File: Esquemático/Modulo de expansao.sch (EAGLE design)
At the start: 77 parts, among them K1 AQYAQY27, K2 AQYAQY27, K3 AQYAQY27, K4 AQYAQY27, K5 AQYAQY27, K6 AQYAQY27, U3 LM1117-3.3V

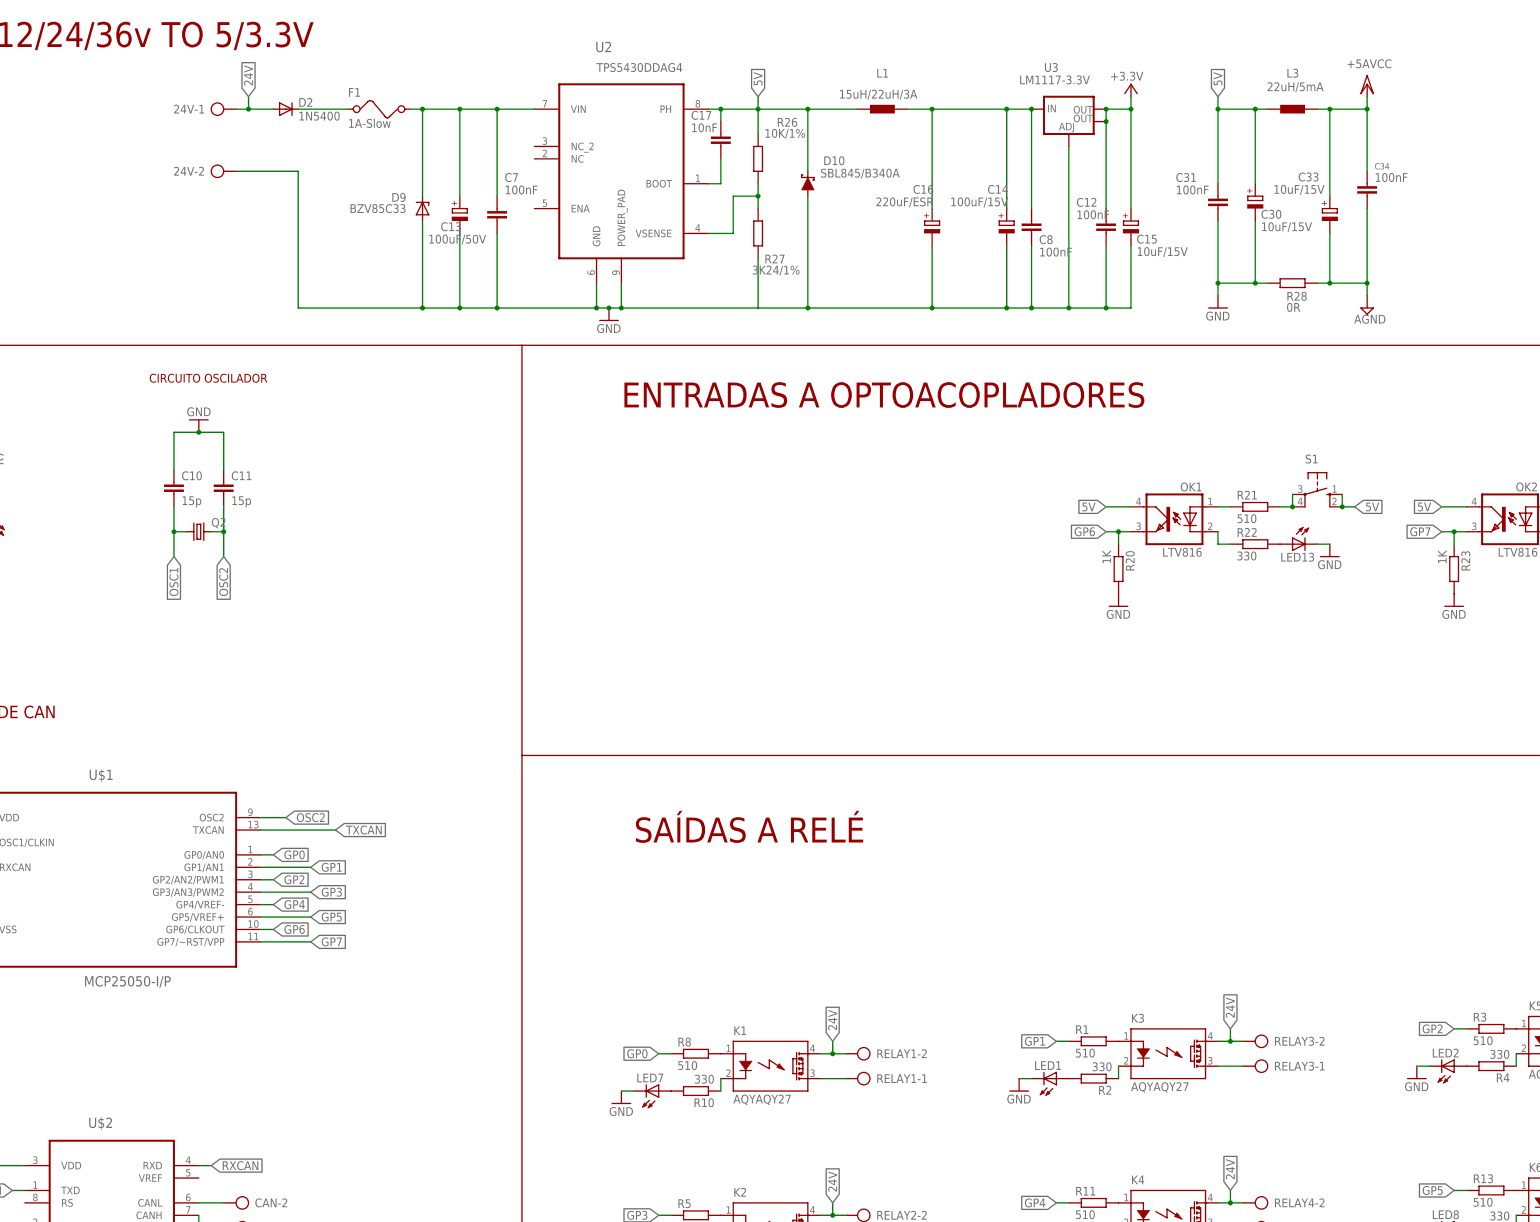
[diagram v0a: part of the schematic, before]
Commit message: Correçao no modulo de expansao e alteraçao de nomes dos ficheiros
No modulo de expansao, passei tudo para thro hole e comecei já a fazer
pcb. enviei para o isaias por email para ver se quer alterar alguma
coisa
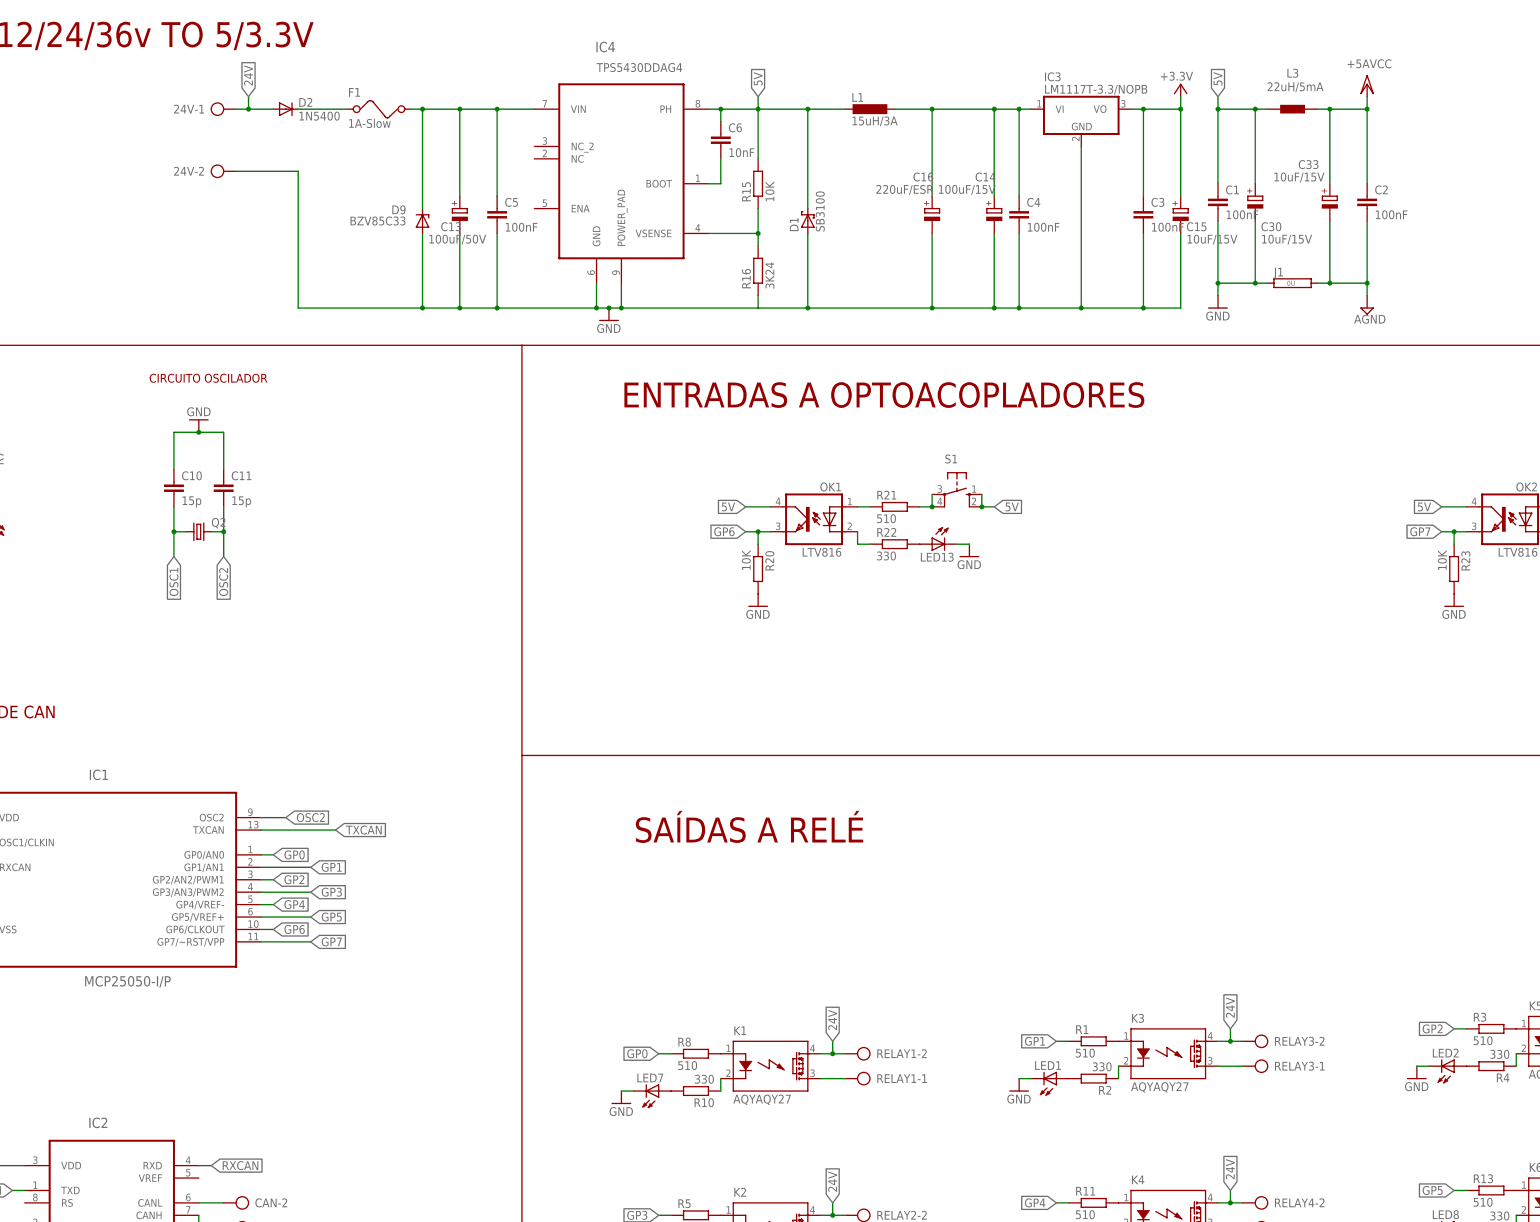
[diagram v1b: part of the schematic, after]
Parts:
- removed C12, C31, C34, C7, C8: 100nF, rcl:C-EUC0805
- removed C17: 10nF, rcl:C-EUC0805
- removed D10: SBL845/B340A, SparkFun-DiscreteSemi:DIODE-SCHOTTKY-B340A
- removed R26: 10K/1%, rcl:R-EU_R0603
- removed R27: 3K24/1%, rcl:R-EU_R0603
- removed R28: 0R, rcl:R-EU_R0603
- removed U3: LM1117-3.3V, SparkFun-IC-Power:V_REG_LM1117SOT223
- added C1, C2, C3, C4, C5: 100nF, rcl:C-EU050-024X044
- added C6: 10nF, rcl:C-EU075-032X103
- added D1: SB3100, diode:1N5908
- added IC3: LM1117T-3.3/NOPB, linear:LM340H-12
- added J1: (no value), jumper:0R
- added R15: 10K, rcl:R-EU_0204/7
- added R16: 3K24, rcl:R-EU_0204/7
- L1: value 15uH/22uH/3A -> 15uH/3A; device inductors:DR1030 -> rcl:L-EUTJ3-U1
- R20, R23: value 1K -> 10K
- renumbered U$1 to IC1, U$2 to IC2, U2 to IC4
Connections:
- net +3.3V: now also C3.1, IC3.VO; no longer C12.1, U3.OUT, U3.OUT@1
- net 5V: now also C1.1, C6.1, D1.C, L1.2, R15.2; no longer C17.1, C31.1, D10.C, L1.1, R26.1
- net AGND: now also C2.2, J1.2; no longer C34.2, R28.2
- net GND: now also C1.2, C3.2, C4.2, C5.2, D1.A, IC3.GND, J1.1, R16.1; no longer C12.2, C31.2, C7.2, C8.2, D10.A, R27.2, R28.1, U3.ADJ
- net N$21: now also C5.1; no longer C7.1
- net N$65: now also C4.1, IC3.VI, L1.1; no longer C8.1, L1.2, U3.IN
- net N$66: now also C6.2; no longer C17.2
- net N$67: now also R15.1, R16.2; no longer R26.2, R27.1
- net VCC/2: now also C2.1; no longer C34.1
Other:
- moved on the sheet: C14, C15, C16, C33, D9, L1, LED13, OK1, R20, R21, R22, S1

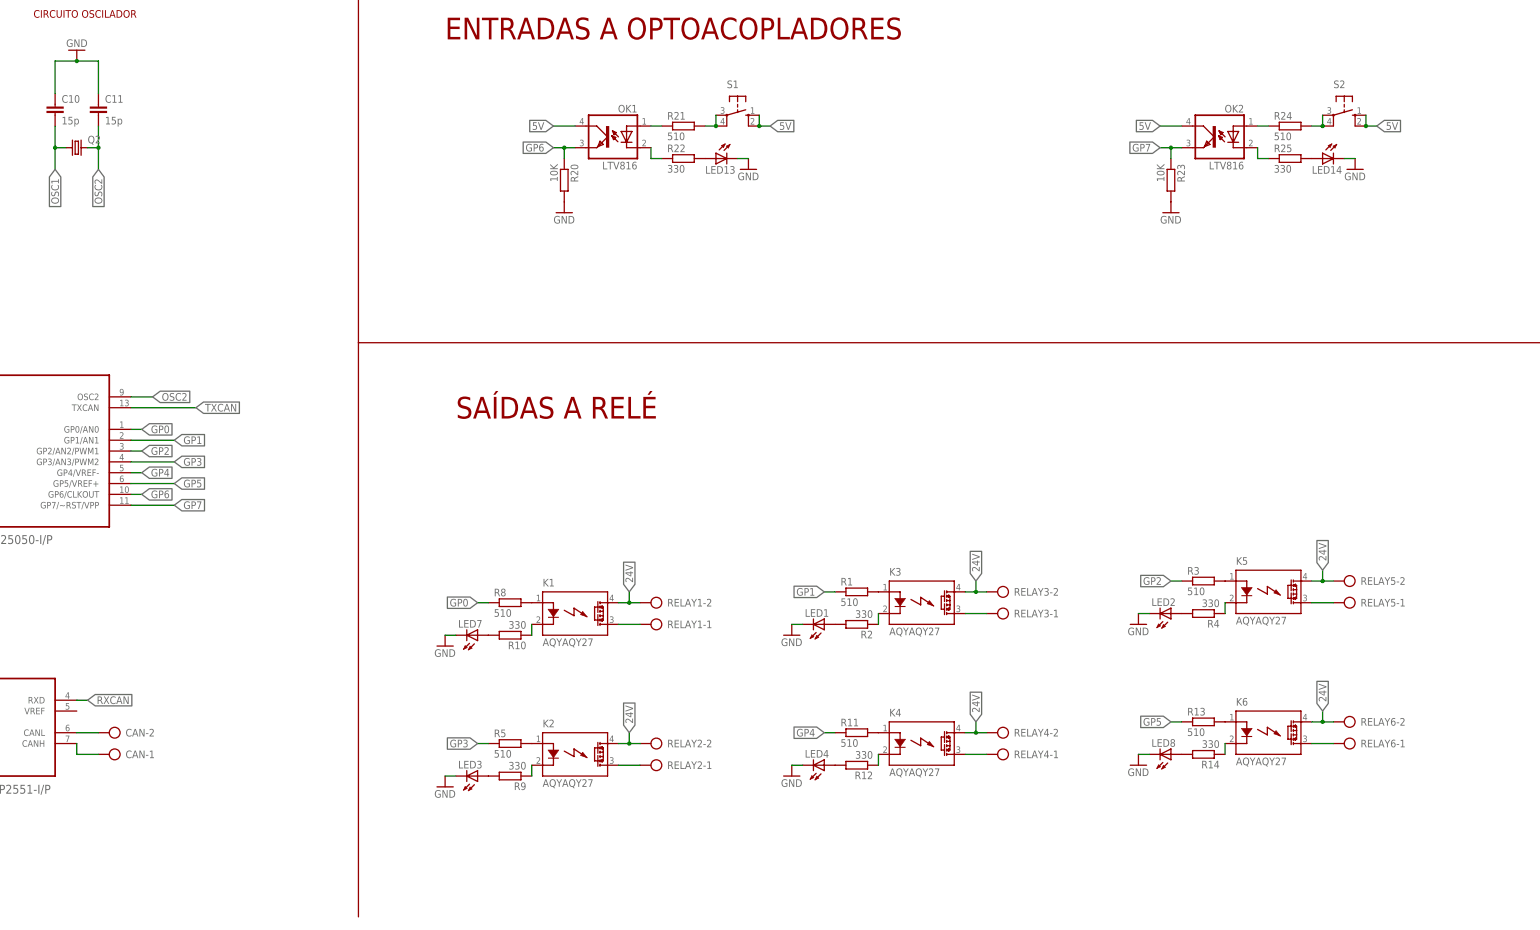
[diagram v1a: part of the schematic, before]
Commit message: alteraçao modulo expansao
Ainda em falta sinalizaçao nas entradas a optos, de resto tudo OK
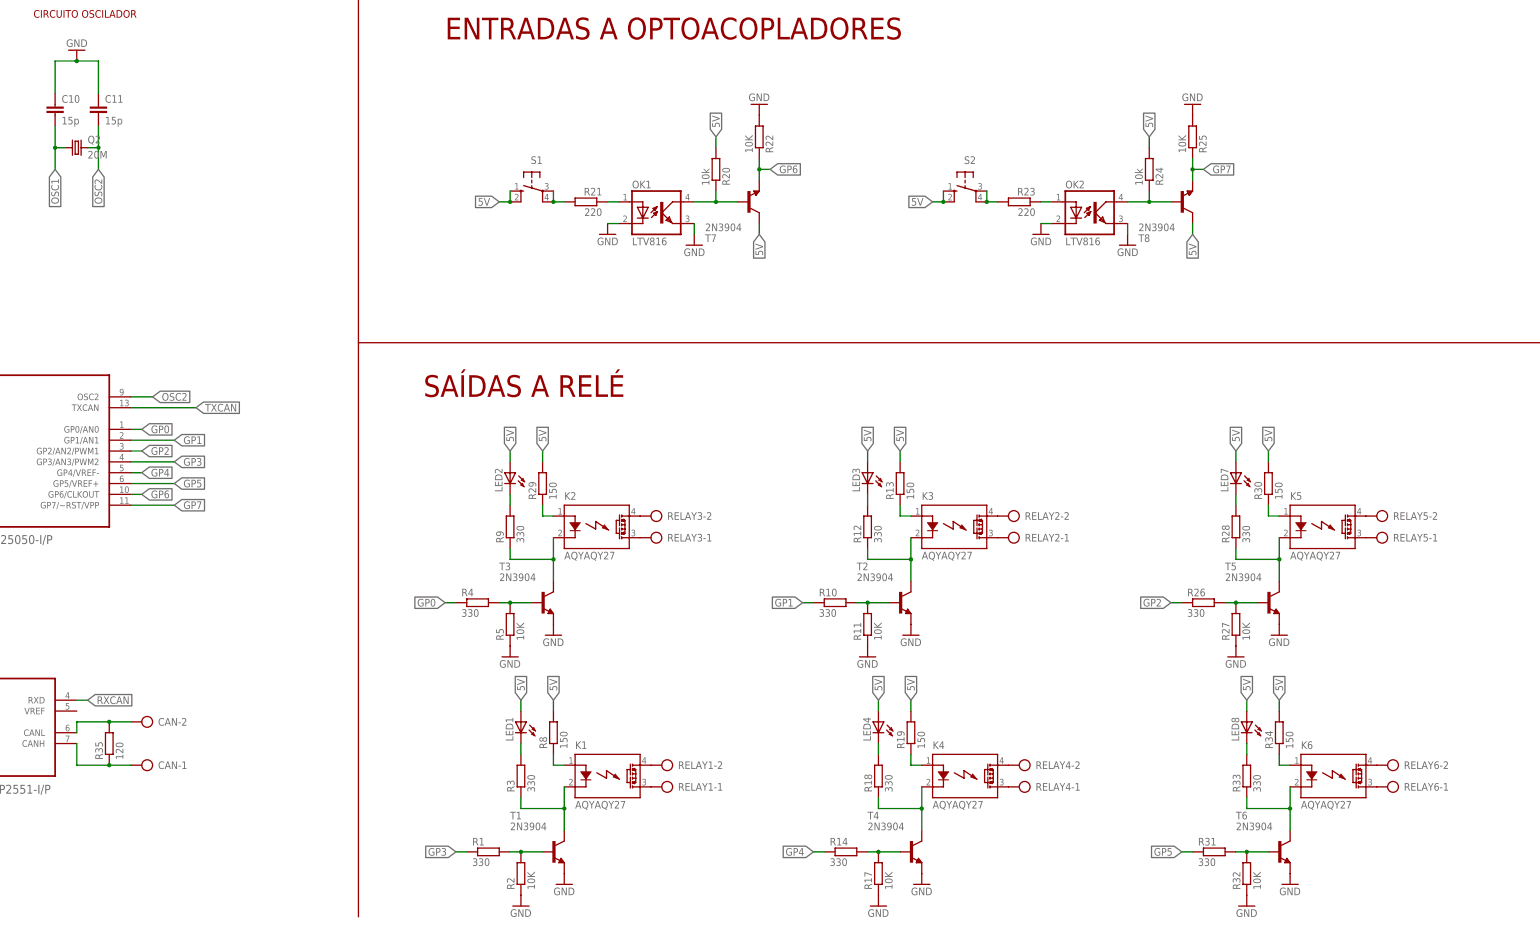
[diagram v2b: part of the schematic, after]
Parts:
- removed LED13, LED14: (no value), led:LED3MM
- added R17, R27, R32: 10K, rcl:R-EU_0204/5
- added R18, R26, R28, R31, R33: 330, rcl:R-EU_0204/5
- added R19, R29, R30, R34: 150, rcl:R-EU_0204/5
- added R35: 120, rcl:R-EU_0204/5
- added T1, T2, T3, T4, T5, T6, T7, T8: 2N3904, transistor:2N3904
- Q2: value (none) -> 20M
- R1, R3: value 510 -> 330
- R11, R5: value 510 -> 10K
- R13, R8: value 510 -> 150
- R2, R22, R25: value 330 -> 10K
- R20: value 10K -> 10k
- R21: value 510 -> 220
- R23: value 10K -> 220
- R24: value 510 -> 10k
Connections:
- removed net N$19 (its old number): K6.A, R13.2
- removed net N$4 (its old number): LED1.A, R2.2
- removed net N$58: R24.2, S2.P, S2.P1
- removed net N$60: LED13.A, R22.2
- removed net N$61: OK1.C, R22.1
- removed net N$62: OK2.A, R24.1
- removed net N$63: LED14.A, R25.2
- removed net N$64: OK2.C, R25.1
- new net N$10: R4.2, R5.2, T3.B
- new net N$18: R14.2, R17.2, T4.B
- new net N$27: R26.2, R27.2, T5.B
- new net N$29: K5.DS1, RELAY5-2.KL
- new net N$3: R1.2, R2.2, T1.B
- new net N$30: LED8.C, R33.2
- new net N$34: R31.2, R32.2, T6.B
- new net N$36: K6.DS1, RELAY6-2.KL
- new net N$37: OK1.COL, R20.1, T7.B
- new net N$38: R23.2, S2.P, S2.P1
- new net N$39: OK2.A, R23.1
- new net N$40: OK2.COL, R24.1, T8.B
- net 24V: no longer K1.DS1, K2.DS1, K3.DS1, K4.DS1, K5.DS1, K6.DS1, RELAY1-2.KL, RELAY2-2.KL, RELAY3-2.KL, RELAY4-2.KL, RELAY5-2.KL, RELAY6-2.KL
- net 5V: now also K1.A, K2.A, K3.A, K4.A, K5.A, K6.A, LED1.A, LED2.A, LED3.A, LED4.A, LED7.A, LED8.A, R13.1, R13.2, R19.1, R19.2, R20.2, R24.2, R29.1, R29.2, R30.1, R30.2, R34.1, R34.2, R8.1, R8.2, T7.C, T8.C; no longer OK1.COL, OK2.COL
- net GND: now also OK1.C, OK1.EMIT, OK2.C, OK2.EMIT, R11.1, R17.1, R2.1, R22.2, R25.2, R27.1, R32.1, R5.1, T1.E, T2.E, T3.E, T4.E, T5.E, T6.E; no longer LED1.C, LED13.C, LED14.C, LED2.C, LED3.C, LED4.C, LED7.C, LED8.C, R20.2, R23.2
- net GP0: now also R4.1; no longer R8.1
- net GP1: now also R10.1; no longer R1.1
- net GP2: now also R26.1; no longer R3.1
- net GP3: now also R1.1; no longer R5.1
- net GP4: now also R14.1; no longer R11.1
- net GP5: now also R31.1; no longer R13.1
- net GP6: now also R22.1, T7.E; no longer OK1.EMIT, R20.1
- net GP7: now also R25.1, T8.E; no longer OK2.EMIT, R23.1
- net N$1: now also LED1.C, R3.2; no longer K1.K, R10.1
- net N$11: now also LED2.C, R9.2; no longer K2.A, R5.2
- net N$12: now also K2.K, R9.1, T3.C; no longer LED3.A, R9.2
- net N$13: now also K2.DS2, RELAY3-1.KL; no longer K2.K, R9.1
- net N$14: now also K2.DS1, RELAY3-2.KL; no longer K2.DS2, RELAY2-1.KL
- net N$15: now also K3.DS1, RELAY2-2.KL; no longer K4.A, R11.2
- net N$16: now also LED4.C, R18.2; no longer LED4.A, R12.2
- net N$17: now also R18.1, T4.C; no longer R12.1
- net N$2: now also K1.K, R3.1, T1.C; no longer K3.A, R1.2
- net N$20: now also K4.DS1, RELAY4-2.KL; no longer LED8.A, R14.2
- net N$22: now also LED7.C, R28.2; no longer K1.A, R8.2
- net N$26: now also K5.K, R28.1, T5.C; no longer K6.K, R14.1
- net N$31: now also R35.2
- net N$32: now also R35.1
- net N$33: now also K6.K, R33.1, T6.C; no longer LED7.A, R10.2
- net N$5: now also K1.DS1, RELAY1-2.KL; no longer K3.K, R2.1
- net N$6: now also LED3.C, R12.2; no longer K3.DS2, RELAY3-1.KL
- net N$7: now also K3.K, R12.1, T2.C; no longer K5.A, R3.2
- net N$8: now also R10.2, R11.2, T2.B; no longer LED2.A, R4.2
- net N$9: now also K3.DS2, RELAY2-1.KL; no longer K5.K, R4.1
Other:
- moved on the sheet: CAN-1, CAN-2, K1, K2, K3, K4, K5, K6, LED1, LED2, LED3, LED4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
